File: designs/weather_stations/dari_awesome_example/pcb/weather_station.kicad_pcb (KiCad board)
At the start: 2 copper layers, 78 x 52 mm, 25 parts, among them J1 ST7735, J2 NEOPIXEL, J3 DHT22, J4 UART, SW1 F TO C, U1 WEMOS C3 MINI

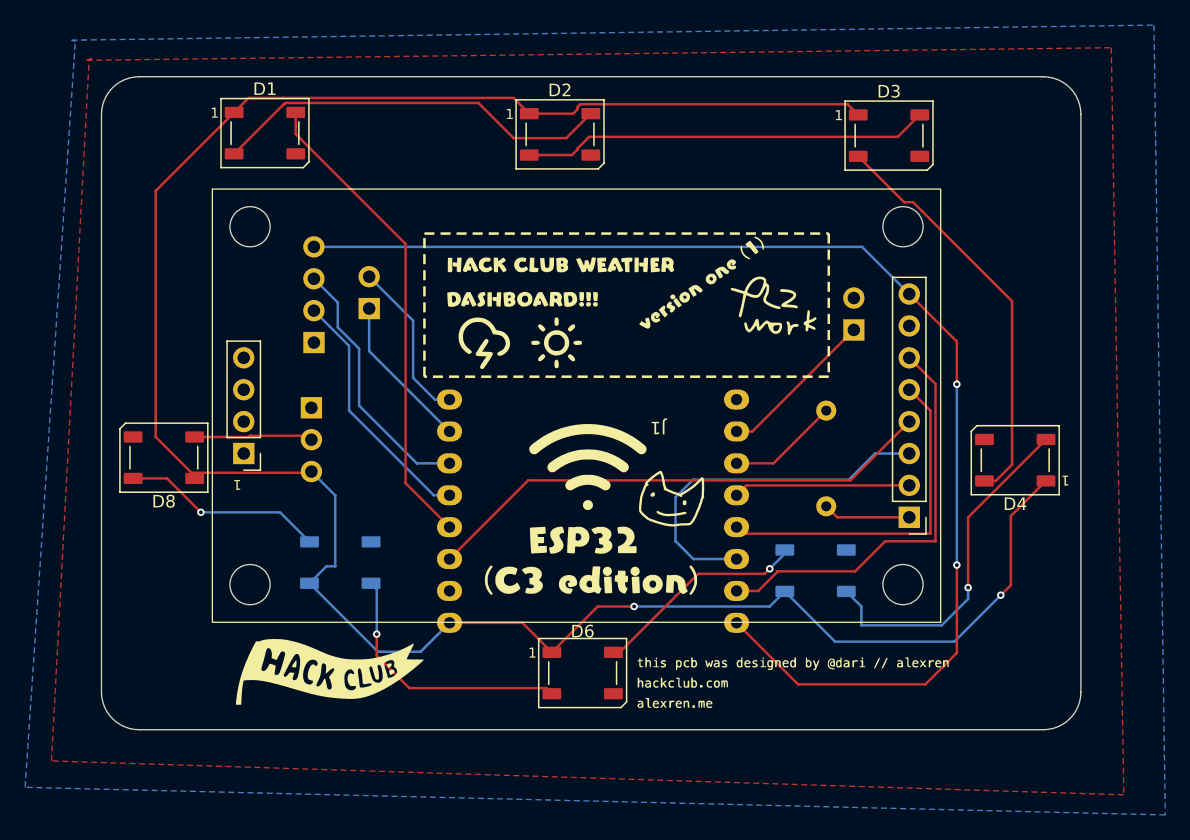
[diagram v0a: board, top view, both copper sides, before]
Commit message: updated weather station example
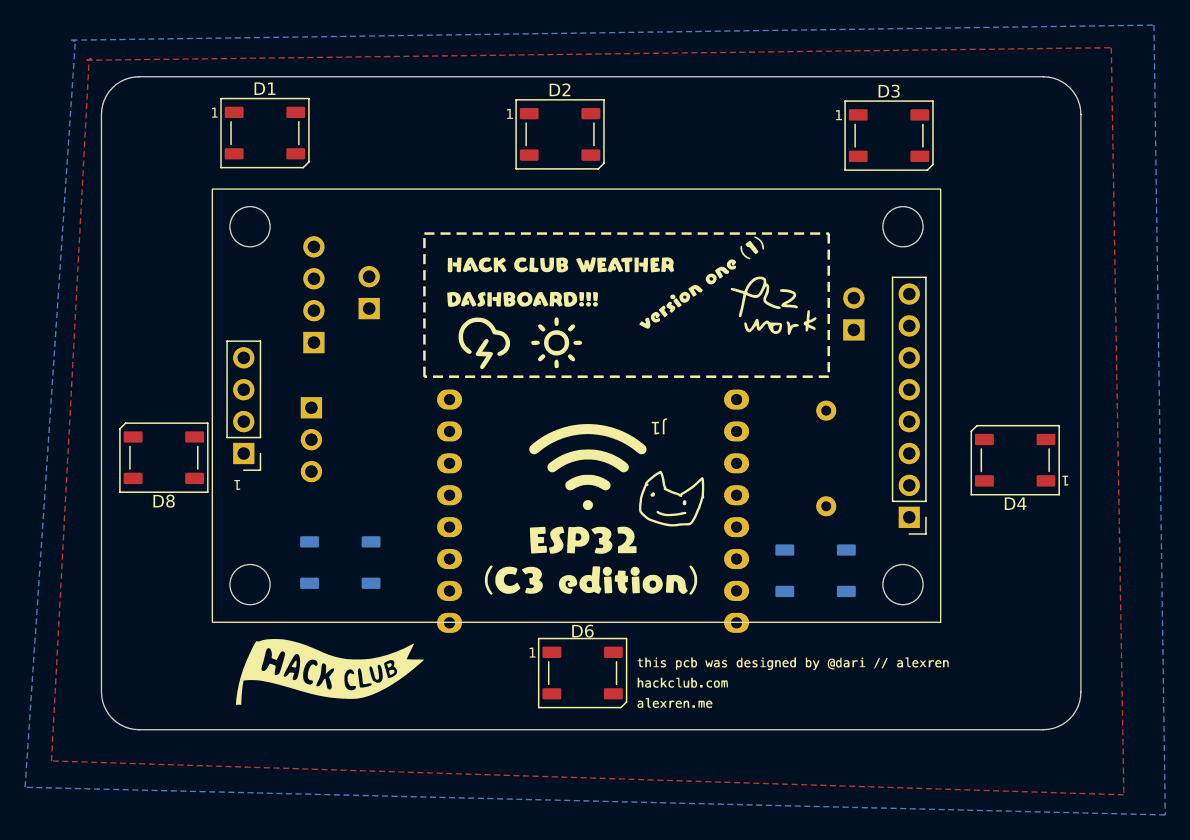
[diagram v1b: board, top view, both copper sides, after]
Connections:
- J1 pad 1: Net-(J1-Pin_1) -> +3V3
- J1 pad 2: SCK -> GND
- J1 pad 3: MOSI -> CS
- J1 pad 4: D/C -> RST
- J1 pad 5: RST -> D/C
- J1 pad 6: CS -> MOSI
- J1 pad 7: GND -> SCK
- J1 pad 8: +3V3 -> Net-(J1-Pin_8)
- R1 pad 2: Net-(J1-Pin_1) -> Net-(J1-Pin_8)
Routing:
- net +5V: track 179.5 -> 0.00 mm, vias 2 -> 0
- net +3V3: track 99.8 -> 0.00 mm, vias 2 -> 0
- net D/C: track 41.1 -> 0.00 mm
- net NEOPIXEL: track 38.1 -> 0.00 mm
- net CS: track 33.0 -> 0.00 mm
- net Net-(D3-DOUT): track 32.8 -> 0.00 mm
- net Net-(D2-DOUT): track 32.5 -> 0.00 mm
- net Net-(D1-DOUT): track 32.0 -> 0.00 mm
- net MOSI: track 29.0 -> 0.00 mm
- net Net-(D4-DOUT): track 27.8 -> 0.00 mm, vias 1 -> 0
- net RST: track 27.8 -> 0.00 mm
- net Net-(D6-DOUT): track 21.1 -> 0.00 mm, vias 1 -> 0
- net SCL: track 20.7 -> 0.00 mm
- net SDA: track 19.9 -> 0.00 mm
- net Net-(D5-DOUT): track 17.2 -> 0.00 mm, vias 1 -> 0
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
